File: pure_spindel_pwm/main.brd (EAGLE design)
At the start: 26.7 x 12.1 mm, 8 parts, among them J1 SPINDEL, J2 POWER, J3 CONTROL, Q1 IRF530, U1 IR2117SO8-2

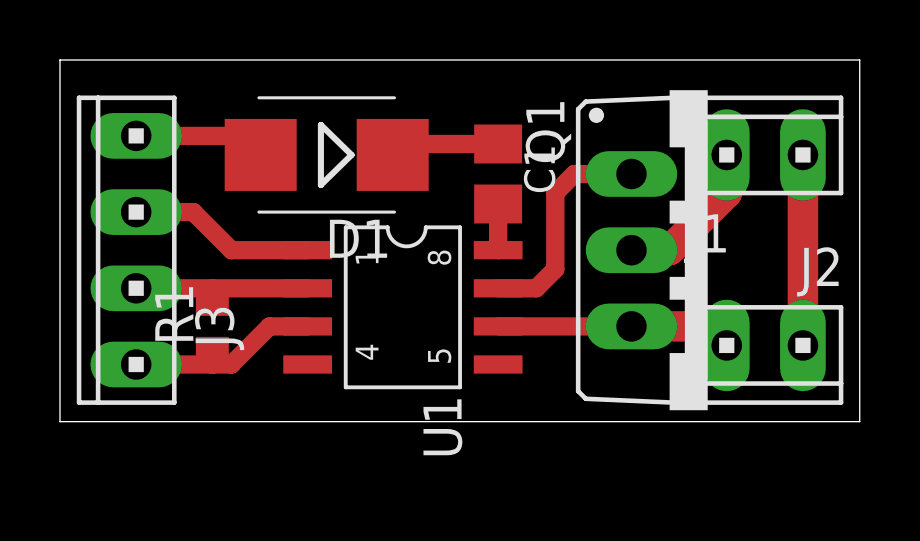
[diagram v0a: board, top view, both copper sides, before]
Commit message: pure_spindel_pwm: fix: invalid capacitor nets
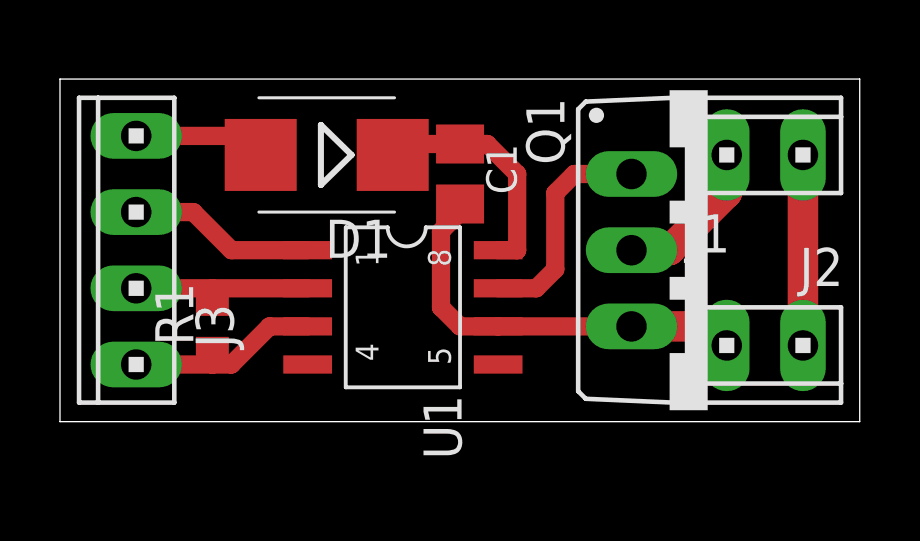
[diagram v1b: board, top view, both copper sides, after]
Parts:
- moved C1 1.27 mm to (13.3, 8.26)
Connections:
- removed net N$1: C1.1, D1.C
- net GND_48V: now also C1.2
- net VB: now also C1.1, D1.C; no longer C1.2
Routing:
- net VB: track 1.54 -> 8.29 mm
- net GND_48V: track 7.88 -> 13.8 mm
- net N$1: track 3.67 -> 0.00 mm
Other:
- board size 26.7 x 12.1 mm -> 26.7 x 11.4 mm
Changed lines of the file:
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@@
 <plain>
 <wire x1="0" y1="0" x2="26.6575" y2="0" width="0" layer="20"/>
-<wire x1="26.6575" y1="0" x2="26.6575" y2="12.055" width="0" layer="20"/>
-<wire x1="26.6575" y1="12.055" x2="0" y2="12.055" width="0" layer="20"/>
-<wire x1="0" y1="12.055" x2="0" y2="0" width="0" layer="20"/>
+<wire x1="26.6575" y1="0" x2="26.6575" y2="11.42" width="0" layer="20"/>
+<wire x1="26.6575" y1="11.42" x2="0" y2="11.42" width="0" layer="20"/>
+<wire x1="0" y1="11.42" x2="0" y2="0" width="0" layer="20"/>
 </plain>
 <attributes>
@@
 </autorouter>
 <elements>
-<element name="C1" library="rcl" library_urn="urn:adsk.eagle:library:334" package="C0805K" package3d_urn="urn:adsk.eagle:package:23681/2" value="0.1uf" x="14.605" y="8.255" rot="R270">
-<attribute name="SPICEPREFIX" value="C" x="14.605" y="8.255" size="1.778" layer="27" rot="R270" display="off"/>
+<element name="C1" library="rcl" library_urn="urn:adsk.eagle:library:334" package="C0805K" package3d_urn="urn:adsk.eagle:package:23681/2" value="0.1uf" x="13.335" y="8.255" rot="R270">
+<attribute name="SPICEPREFIX" value="C" x="13.335" y="8.255" size="1.778" layer="27" rot="R270" display="off"/>
 </element>
 <element name="D1" library="diode" library_urn="urn:adsk.eagle:library:210" package="SMB" package3d_urn="urn:adsk.eagle:package:43404/2" value="ES1D" x="8.89" y="8.89" rot="R180"/>
@@
 </elements>
 <signals>
-<signal name="VB">
-<contactref element="U1" pad="8"/>
-<contactref element="C1" pad="2"/>
-<wire x1="14.605" y1="5.715" x2="14.605" y2="7.255" width="0.6096" layer="1"/>
-</signal>
-<signal name="N$1">
-<contactref element="C1" pad="1"/>
-<contactref element="D1" pad="C"/>
-<wire x1="14.605" y1="9.255" x2="11.455" y2="9.255" width="0.6096" layer="1"/>
-<wire x1="11.455" y1="9.255" x2="11.09" y2="8.89" width="0.6096" layer="1"/>
-</signal>
 <signal name="GATE">
 <contactref element="U1" pad="7"/>
@@
 <wire x1="22.225" y1="2.54" x2="21.59" y2="3.175" width="1.016" layer="1"/>
 <wire x1="21.59" y1="3.175" x2="19.05" y2="3.175" width="1.016" layer="1"/>
+<contactref element="C1" pad="2"/>
+<wire x1="14.605" y1="3.175" x2="13.335" y2="3.175" width="0.6096" layer="1"/>
+<wire x1="13.335" y1="3.175" x2="12.7" y2="3.81" width="0.6096" layer="1"/>
+<wire x1="12.7" y1="3.81" x2="12.7" y2="6.35" width="0.6096" layer="1"/>
+<wire x1="12.7" y1="6.35" x2="13.335" y2="6.985" width="0.6096" layer="1"/>
+<wire x1="13.335" y1="6.985" x2="13.335" y2="7.255" width="0.6096" layer="1"/>
 </signal>
 <signal name="VCC_5V">
@@
 <wire x1="24.765" y1="8.89" x2="24.765" y2="2.54" width="1.016" layer="1"/>
 </signal>
+<signal name="VB">
+<contactref element="U1" pad="8"/>
+<contactref element="D1" pad="C"/>
+<contactref element="C1" pad="1"/>
+<wire x1="14.24" y1="9.255" x2="15.24" y2="8.255" width="0.6096" layer="1"/>
+<wire x1="14.24" y1="9.255" x2="13.335" y2="9.255" width="0.6096" layer="1"/>
+<wire x1="15.24" y1="5.715" x2="14.605" y2="5.715" width="0.6096" layer="1"/>
+<wire x1="15.24" y1="8.255" x2="15.24" y2="5.715" width="0.6096" layer="1"/>
+<wire x1="13.335" y1="9.255" x2="11.7" y2="9.255" width="0.6096" layer="1"/>
+<wire x1="11.7" y1="9.255" x2="11.43" y2="9.525" width="0.6096" layer="1"/>
+<wire x1="11.43" y1="9.525" x2="11.09" y2="9.185" width="0.6096" layer="1"/>
+<wire x1="11.09" y1="9.185" x2="11.09" y2="8.89" width="0.6096" layer="1"/>
+</signal>
 </signals>
+<errors>
+</errors>
 </board>
 </drawing>
